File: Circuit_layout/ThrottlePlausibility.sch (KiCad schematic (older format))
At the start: 65 parts, among them Q2 MMBF170, SW2 TS5A3159, U18 TS912, U22 TS372, U23 TLP293, U24 TLP293, U3 MCP6004, U4 MCP6004, U5 LM7810CT, U6 TS912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

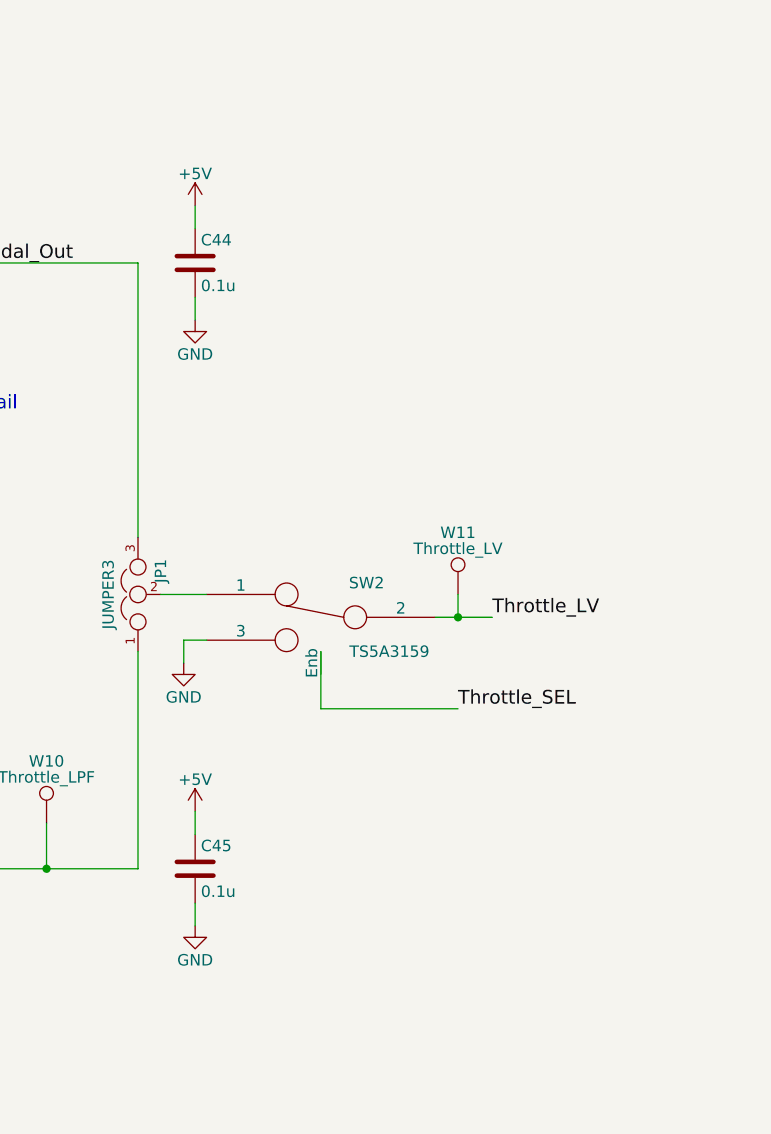
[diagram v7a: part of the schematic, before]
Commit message: fixed switch, added pulldown resistor, added DPDT switch for extra ADCs
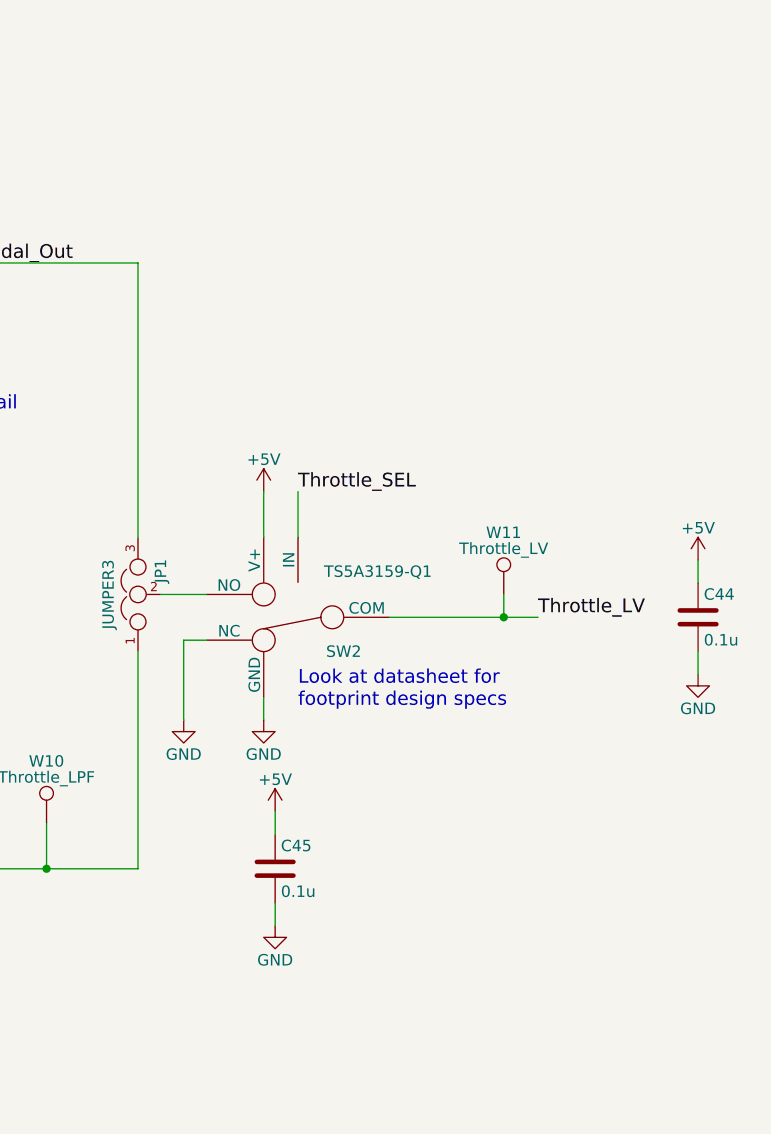
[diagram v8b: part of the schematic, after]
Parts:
- removed SW2: TS5A3159, symbol SWITCH_INV-RESCUE-Circuit_layout
- added SW2: TS5A3159-Q1, TO_SOT_Packages_SMD:SOT-23-6_Handsoldering, symbol TS5A3159-Q1
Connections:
- net +5V: now also SW2.5 (V+)
- net GND: now also SW2.2 (GND), SW2.3 (NC)
- net Throttle_LV: now also SW2.4 (COM)
- net Throttle_SEL: now also SW2.6 (IN)
- net at JP1.2: now also SW2.1 (NO)
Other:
- note added: "Look at datasheet for \nfootprint design specs"
- moved on the sheet: C44, C45, W11
